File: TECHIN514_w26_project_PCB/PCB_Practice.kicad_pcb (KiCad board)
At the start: 2 copper layers, 19 x 18 mm, 12 parts, among them J1 Conn_01x04_Pin, U1 VL53L4CXV0DH_1, U2 MIC5376-2.8YMT-TZ

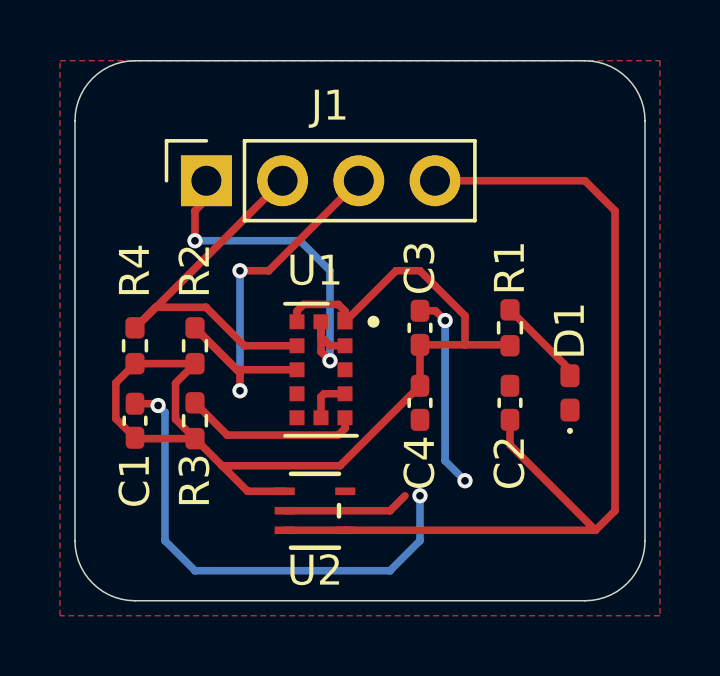
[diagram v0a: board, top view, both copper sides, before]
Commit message: add ground plane to back of pcb
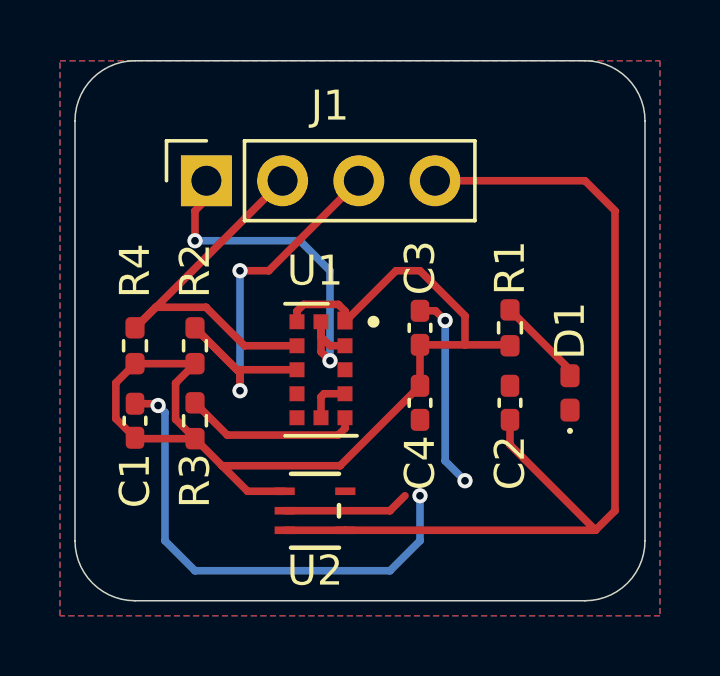
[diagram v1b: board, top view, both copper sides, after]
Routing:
- added copper zone on B.Cu, net GND
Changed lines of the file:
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@@
 		(net 10)
 		(net_name "GND")
-		(layer "F.Cu")
+		(layers "F.Cu" "B.Cu")
 		(hatch edge 0.5)
 		(connect_pads
